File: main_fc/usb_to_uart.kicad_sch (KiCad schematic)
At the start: 8 parts, among them U7 FT232RL

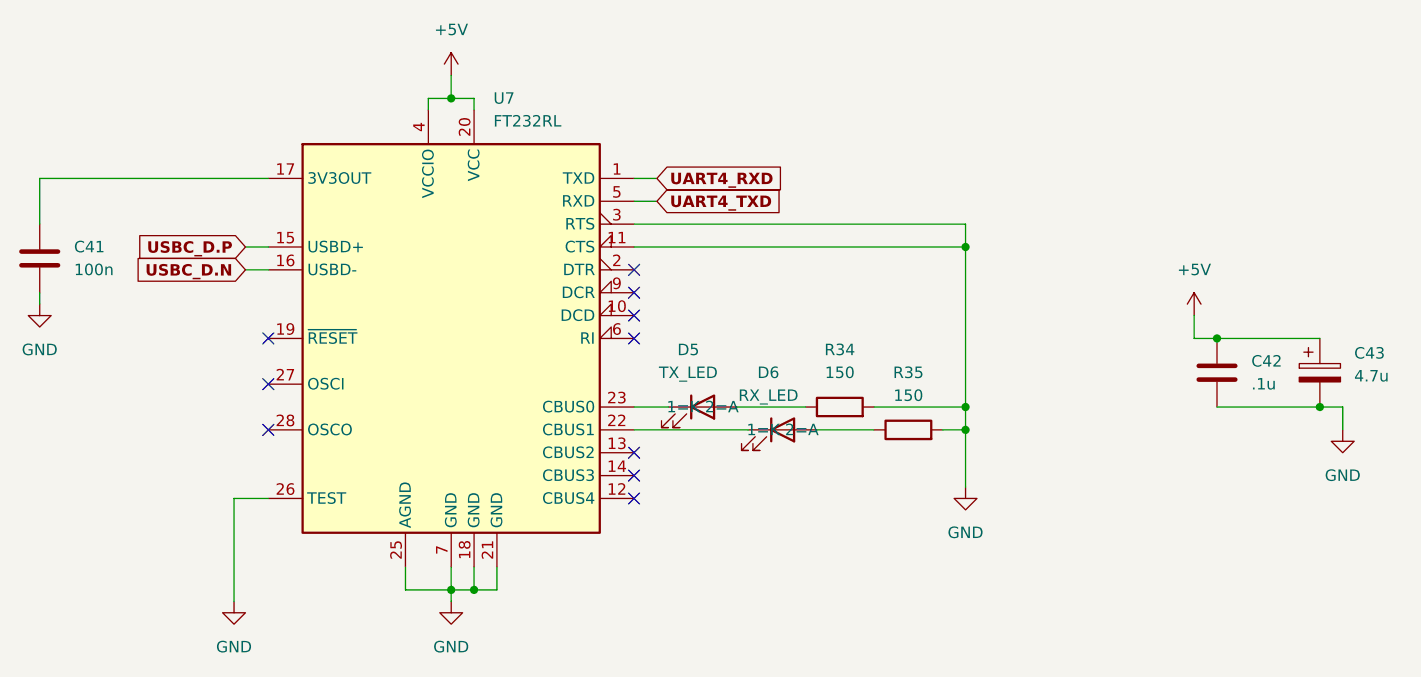
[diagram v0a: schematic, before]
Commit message: main flight computer annotations and passive footprints
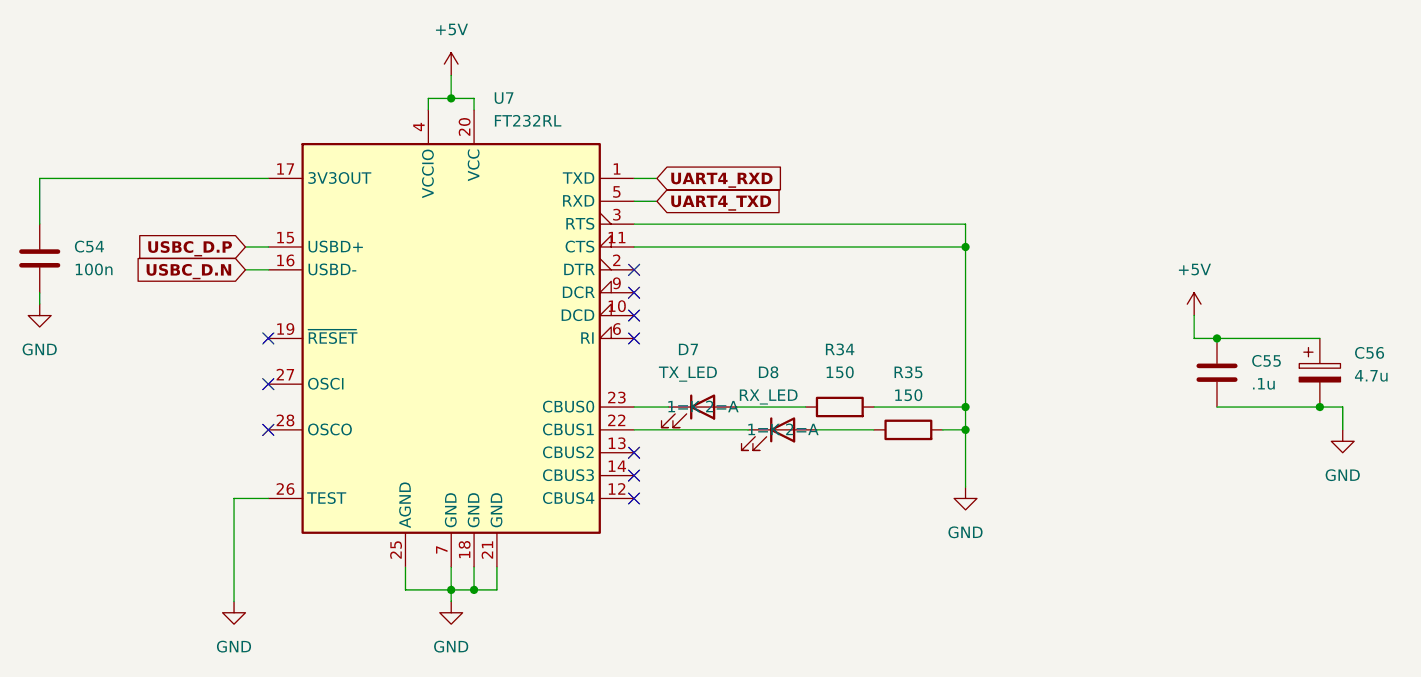
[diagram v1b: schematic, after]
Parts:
- renumbered C41 to C54, C42 to C55, C43 to C56, D5 to D7, D6 to D8
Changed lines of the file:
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@@
 		(dnp no)
 		(fields_autoplaced yes)
-		(property "Reference" "C41"
+		(property "Reference" "C54"
 			(at 78.74 83.8199 0)
 			(effects
@@
 			(project "main_fc"
 				(path "/2e5bfe72-277e-40a6-babb-0928c11aa964/acf68788-bc39-4e66-824a-e6e1af3717de"
-					(reference "C41")
+					(reference "C54")
 					(unit 1)
 				)
@@
 		(dnp no)
 		(fields_autoplaced yes)
-		(property "Reference" "#PWR062"
+		(property "Reference" "#PWR070"
 			(at 203.2 95.25 0)
 			(effects
@@
 			(project "main_fc"
 				(path "/2e5bfe72-277e-40a6-babb-0928c11aa964/acf68788-bc39-4e66-824a-e6e1af3717de"
-					(reference "#PWR062")
+					(reference "#PWR070")
 					(unit 1)
 				)
@@
 		(dnp no)
 		(fields_autoplaced yes)
-		(property "Reference" "C42"
+		(property "Reference" "C55"
 			(at 209.55 96.5199 0)
 			(effects
@@
 			(project "main_fc"
 				(path "/2e5bfe72-277e-40a6-babb-0928c11aa964/acf68788-bc39-4e66-824a-e6e1af3717de"
-					(reference "C42")
+					(reference "C55")
 					(unit 1)
 				)
@@
 		(dnp no)
 		(fields_autoplaced yes)
-		(property "Reference" "D6"
+		(property "Reference" "D8"
 			(at 155.8925 97.79 0)
 			(effects
@@
 			(project "main_fc"
 				(path "/2e5bfe72-277e-40a6-babb-0928c11aa964/acf68788-bc39-4e66-824a-e6e1af3717de"
-					(reference "D6")
+					(reference "D8")
 					(unit 1)
 				)
@@
 		(dnp no)
 		(fields_autoplaced yes)
-		(property "Reference" "#PWR058"
+		(property "Reference" "#PWR066"
 			(at 96.52 129.54 0)
 			(effects
@@
 			(project "main_fc"
 				(path "/2e5bfe72-277e-40a6-babb-0928c11aa964/acf68788-bc39-4e66-824a-e6e1af3717de"
-					(reference "#PWR058")
+					(reference "#PWR066")
 					(unit 1)
 				)
@@
 		(dnp no)
 		(fields_autoplaced yes)
-		(property "Reference" "D5"
+		(property "Reference" "D7"
 			(at 147.0025 95.25 0)
 			(effects
@@
 			(project "main_fc"
 				(path "/2e5bfe72-277e-40a6-babb-0928c11aa964/acf68788-bc39-4e66-824a-e6e1af3717de"
-					(reference "D5")
+					(reference "D7")
 					(unit 1)
 				)
@@
 		(dnp no)
 		(fields_autoplaced yes)
-		(property "Reference" "#PWR063"
+		(property "Reference" "#PWR071"
 			(at 219.71 110.49 0)
 			(effects
@@
 			(project "main_fc"
 				(path "/2e5bfe72-277e-40a6-babb-0928c11aa964/acf68788-bc39-4e66-824a-e6e1af3717de"
-					(reference "#PWR063")
+					(reference "#PWR071")
 					(unit 1)
 				)
@@
 		(dnp no)
 		(fields_autoplaced yes)
-		(property "Reference" "#PWR057"
+		(property "Reference" "#PWR065"
 			(at 74.93 96.52 0)
 			(effects
@@
 			(project "main_fc"
 				(path "/2e5bfe72-277e-40a6-babb-0928c11aa964/acf68788-bc39-4e66-824a-e6e1af3717de"
-					(reference "#PWR057")
+					(reference "#PWR065")
 					(unit 1)
 				)
@@
 		(dnp no)
 		(fields_autoplaced yes)
-		(property "Reference" "#PWR061"
+		(property "Reference" "#PWR069"
 			(at 177.8 116.84 0)
 			(effects
@@
 			(project "main_fc"
 				(path "/2e5bfe72-277e-40a6-babb-0928c11aa964/acf68788-bc39-4e66-824a-e6e1af3717de"
-					(reference "#PWR061")
+					(reference "#PWR069")
 					(unit 1)
 				)
@@
 		(dnp no)
 		(fields_autoplaced yes)
-		(property "Reference" "#PWR060"
+		(property "Reference" "#PWR068"
 			(at 120.65 129.54 0)
 			(effects
@@
 			(project "main_fc"
 				(path "/2e5bfe72-277e-40a6-babb-0928c11aa964/acf68788-bc39-4e66-824a-e6e1af3717de"
-					(reference "#PWR060")
+					(reference "#PWR068")
 					(unit 1)
 				)
@@
 		(dnp no)
 		(fields_autoplaced yes)
-		(property "Reference" "C43"
+		(property "Reference" "C56"
 			(at 220.98 95.6309 0)
 			(effects
@@
 			(project "main_fc"
 				(path "/2e5bfe72-277e-40a6-babb-0928c11aa964/acf68788-bc39-4e66-824a-e6e1af3717de"
-					(reference "C43")
+					(reference "C56")
 					(unit 1)
 				)
@@
 		(dnp no)
 		(fields_autoplaced yes)
-		(property "Reference" "#PWR059"
+		(property "Reference" "#PWR067"
 			(at 120.65 68.58 0)
 			(effects
@@
 			(project "main_fc"
 				(path "/2e5bfe72-277e-40a6-babb-0928c11aa964/acf68788-bc39-4e66-824a-e6e1af3717de"
-					(reference "#PWR059")
-					(unit 1)
-				)
+					(reference "#PWR067")
+					(unit 1)
+				)

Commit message: added new stm symbol/footprint
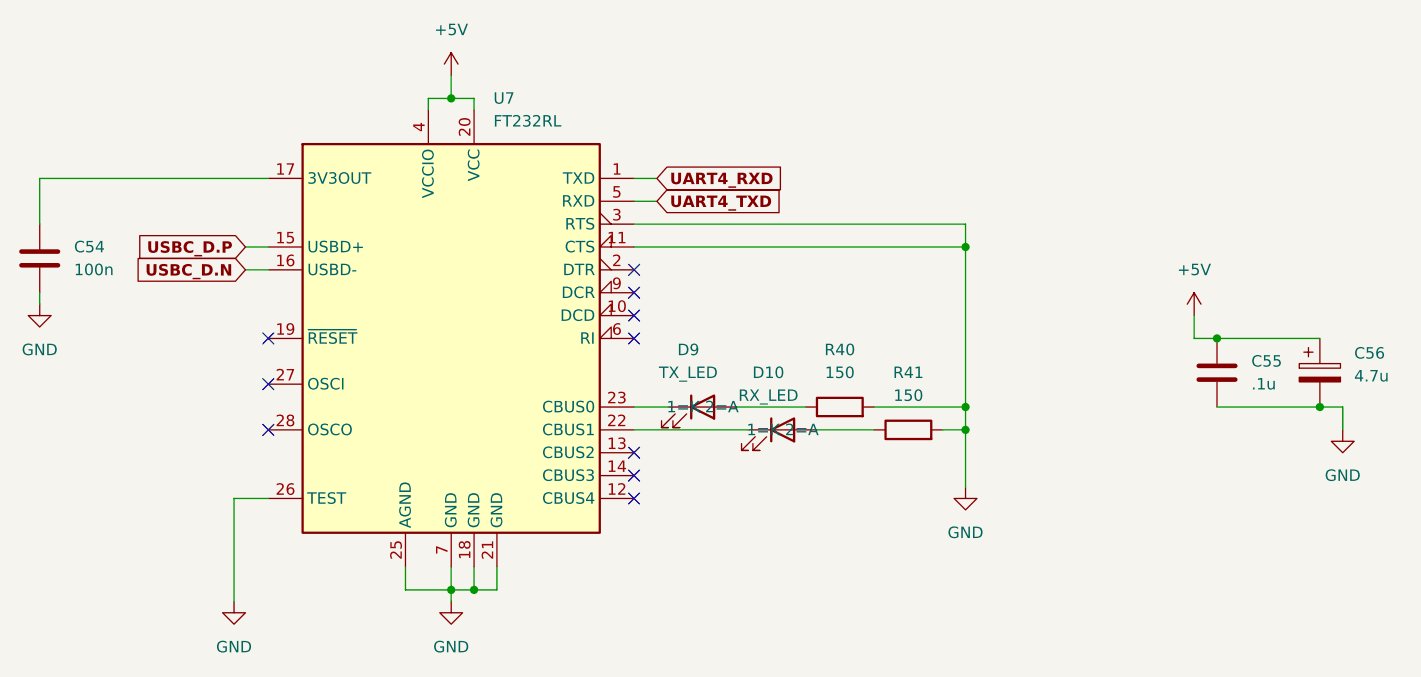
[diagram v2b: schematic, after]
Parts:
- renumbered D8 to D10, D7 to D9, R34 to R40, R35 to R41
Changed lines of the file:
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@@
 		(dnp no)
 		(fields_autoplaced yes)
-		(property "Reference" "#PWR070"
+		(property "Reference" "#PWR068"
 			(at 203.2 95.25 0)
 			(effects
@@
 			(project "main_fc"
 				(path "/2e5bfe72-277e-40a6-babb-0928c11aa964/acf68788-bc39-4e66-824a-e6e1af3717de"
-					(reference "#PWR070")
+					(reference "#PWR068")
 					(unit 1)
 				)
@@
 		(dnp no)
 		(fields_autoplaced yes)
-		(property "Reference" "R35"
+		(property "Reference" "R41"
 			(at 171.45 97.79 90)
 			(effects
@@
 			(project "main_fc"
 				(path "/2e5bfe72-277e-40a6-babb-0928c11aa964/acf68788-bc39-4e66-824a-e6e1af3717de"
-					(reference "R35")
+					(reference "R41")
 					(unit 1)
 				)
@@
 		(dnp no)
 		(fields_autoplaced yes)
-		(property "Reference" "D8"
+		(property "Reference" "D10"
 			(at 155.8925 97.79 0)
 			(effects
@@
 			(project "main_fc"
 				(path "/2e5bfe72-277e-40a6-babb-0928c11aa964/acf68788-bc39-4e66-824a-e6e1af3717de"
-					(reference "D8")
+					(reference "D10")
 					(unit 1)
 				)
@@
 		(dnp no)
 		(fields_autoplaced yes)
-		(property "Reference" "#PWR066"
+		(property "Reference" "#PWR064"
 			(at 96.52 129.54 0)
 			(effects
@@
 			(project "main_fc"
 				(path "/2e5bfe72-277e-40a6-babb-0928c11aa964/acf68788-bc39-4e66-824a-e6e1af3717de"
-					(reference "#PWR066")
+					(reference "#PWR064")
 					(unit 1)
 				)
@@
 		(dnp no)
 		(fields_autoplaced yes)
-		(property "Reference" "R34"
+		(property "Reference" "R40"
 			(at 163.83 95.25 90)
 			(effects
@@
 			(project "main_fc"
 				(path "/2e5bfe72-277e-40a6-babb-0928c11aa964/acf68788-bc39-4e66-824a-e6e1af3717de"
-					(reference "R34")
+					(reference "R40")
 					(unit 1)
 				)
@@
 		(dnp no)
 		(fields_autoplaced yes)
-		(property "Reference" "D7"
+		(property "Reference" "D9"
 			(at 147.0025 95.25 0)
 			(effects
@@
 			(project "main_fc"
 				(path "/2e5bfe72-277e-40a6-babb-0928c11aa964/acf68788-bc39-4e66-824a-e6e1af3717de"
-					(reference "D7")
+					(reference "D9")
 					(unit 1)
 				)
@@
 		(dnp no)
 		(fields_autoplaced yes)
-		(property "Reference" "#PWR071"
+		(property "Reference" "#PWR069"
 			(at 219.71 110.49 0)
 			(effects
@@
 			(project "main_fc"
 				(path "/2e5bfe72-277e-40a6-babb-0928c11aa964/acf68788-bc39-4e66-824a-e6e1af3717de"
-					(reference "#PWR071")
+					(reference "#PWR069")
 					(unit 1)
 				)
@@
 		(dnp no)
 		(fields_autoplaced yes)
-		(property "Reference" "#PWR065"
+		(property "Reference" "#PWR063"
 			(at 74.93 96.52 0)
 			(effects
@@
 			(project "main_fc"
 				(path "/2e5bfe72-277e-40a6-babb-0928c11aa964/acf68788-bc39-4e66-824a-e6e1af3717de"
-					(reference "#PWR065")
+					(reference "#PWR063")
 					(unit 1)
 				)
@@
 		(dnp no)
 		(fields_autoplaced yes)
-		(property "Reference" "#PWR069"
+		(property "Reference" "#PWR067"
 			(at 177.8 116.84 0)
 			(effects
@@
 			(project "main_fc"
 				(path "/2e5bfe72-277e-40a6-babb-0928c11aa964/acf68788-bc39-4e66-824a-e6e1af3717de"
-					(reference "#PWR069")
+					(reference "#PWR067")
 					(unit 1)
 				)
@@
 		(dnp no)
 		(fields_autoplaced yes)
-		(property "Reference" "#PWR068"
+		(property "Reference" "#PWR066"
 			(at 120.65 129.54 0)
 			(effects
@@
 			(project "main_fc"
 				(path "/2e5bfe72-277e-40a6-babb-0928c11aa964/acf68788-bc39-4e66-824a-e6e1af3717de"
-					(reference "#PWR068")
+					(reference "#PWR066")
 					(unit 1)
 				)
@@
 		(dnp no)
 		(fields_autoplaced yes)
-		(property "Reference" "#PWR067"
+		(property "Reference" "#PWR065"
 			(at 120.65 68.58 0)
 			(effects
@@
 			(project "main_fc"
 				(path "/2e5bfe72-277e-40a6-babb-0928c11aa964/acf68788-bc39-4e66-824a-e6e1af3717de"
-					(reference "#PWR067")
-					(unit 1)
-				)
+					(reference "#PWR065")
+					(unit 1)
+				)
